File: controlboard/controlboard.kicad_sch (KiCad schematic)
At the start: 34 parts, among them J27 GPIO, J6 Conn_02x04_Counter_Clockwise, SW2 SW_Push TODO FP CHECK

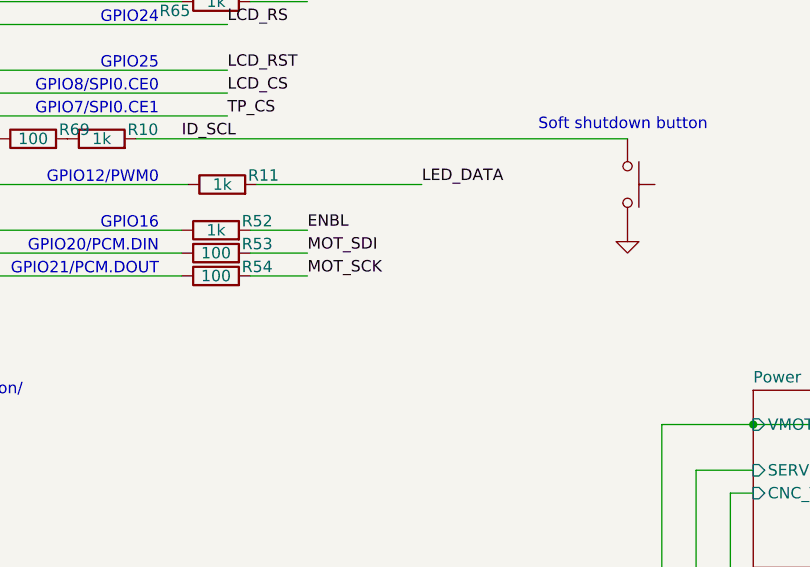
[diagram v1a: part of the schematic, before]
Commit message: Control board changes
Made a few control board changes (green checks on discord)
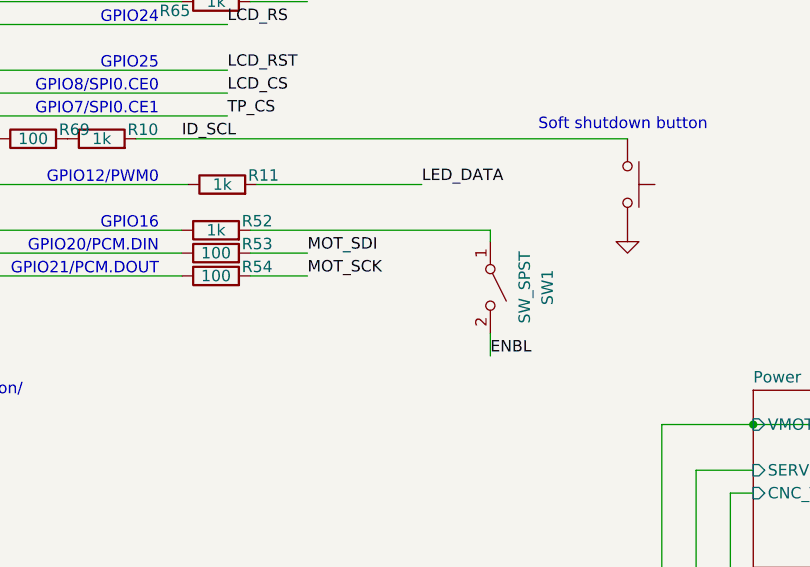
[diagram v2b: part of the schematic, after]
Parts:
- added SW1: SW_SPST, symbol Switch:SW_SPST
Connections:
- net ENBL: now also SW1.2 (B); no longer R52.2
- new net: R52.2, SW1.1 (A)
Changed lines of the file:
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@@
-	(wire
-		(pts
-			(xy 134.62 66.04) (xy 140.97 66.04)
-		)
-		(stroke
-			(width 0)
-			(type solid)
-		)
-	)
 	(wire
 		(pts
@@
 	(wire
 		(pts
+			(xy 161.29 77.47) (xy 161.29 80.01)
+		)
+		(stroke
+			(width 0)
+			(type solid)
+		)
+	)
+	(wire
+		(pts
 			(xy 31.75 66.04) (xy 40.64 66.04)
 		)
@@
 	(wire
 		(pts
+			(xy 161.29 66.04) (xy 134.62 66.04)
+		)
+		(stroke
+			(width 0)
+			(type solid)
+		)
+	)
+	(wire
+		(pts
 			(xy 165.1 125.73) (xy 170.18 125.73)
 		)
@@
 			(width 0)
 			(type default)
+		)
+	)
+	(wire
+		(pts
+			(xy 161.29 67.31) (xy 161.29 66.04)
+		)
+		(stroke
+			(width 0)
+			(type solid)
 		)
 	)
@@
 	)
 	(label "ENBL"
-		(at 140.97 66.04 0)
+		(at 161.29 80.01 0)
 		(fields_autoplaced yes)
 		(effects
@@
 					(unit 1)
 				)
+			)
+		)
+	)
+	(symbol
+		(lib_id "Switch:SW_SPST")
+		(at 161.29 72.39 270)
+		(unit 1)
+		(exclude_from_sim no)
+		(in_bom yes)
+		(on_board yes)
+		(dnp no)
+		(property "Reference" "SW1"
+			(at 167.64 72.39 0)
+			(effects
+				(font
+					(size 1.27 1.27)
+				)
+			)
+		)
+		(property "Value" "SW_SPST"
+			(at 165.1 72.39 0)
+			(effects
+				(font
+					(size 1.27 1.27)
+				)
+			)
+		)
+		(property "Footprint" ""
+			(at 161.29 72.39 0)
+			(effects
+				(font
+					(size 1.27 1.27)
+				)
+				(hide yes)
+			)
+		)
+		(property "Datasheet" "~"
+			(at 161.29 72.39 0)
+			(effects
+				(font
+					(size 1.27 1.27)
+				)
+				(hide yes)
+			)
+		)
+		(property "Description" "Single Pole Single Throw (SPST) switch"
+			(at 161.29 72.39 0)
+			(effects
+				(font
+					(size 1.27 1.27)
+				)
+				(hide yes)
+			)
+		)
+		(pin "1"
+		)
+		(pin "2"
+		)
+		(instances
+			(project ""
+				(path "/2797250d-6fee-4769-b4dd-0e20ce4f0941"
+					(reference "SW1")
+					(unit 1)
+				)
